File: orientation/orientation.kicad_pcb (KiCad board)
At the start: 2 copper layers, 45 x 30 mm, 9 parts, among them J1 Conn_01x02, J2 Conn_01x04, U1 Teensy4.0, U2 STSPIN220, U3 bno055

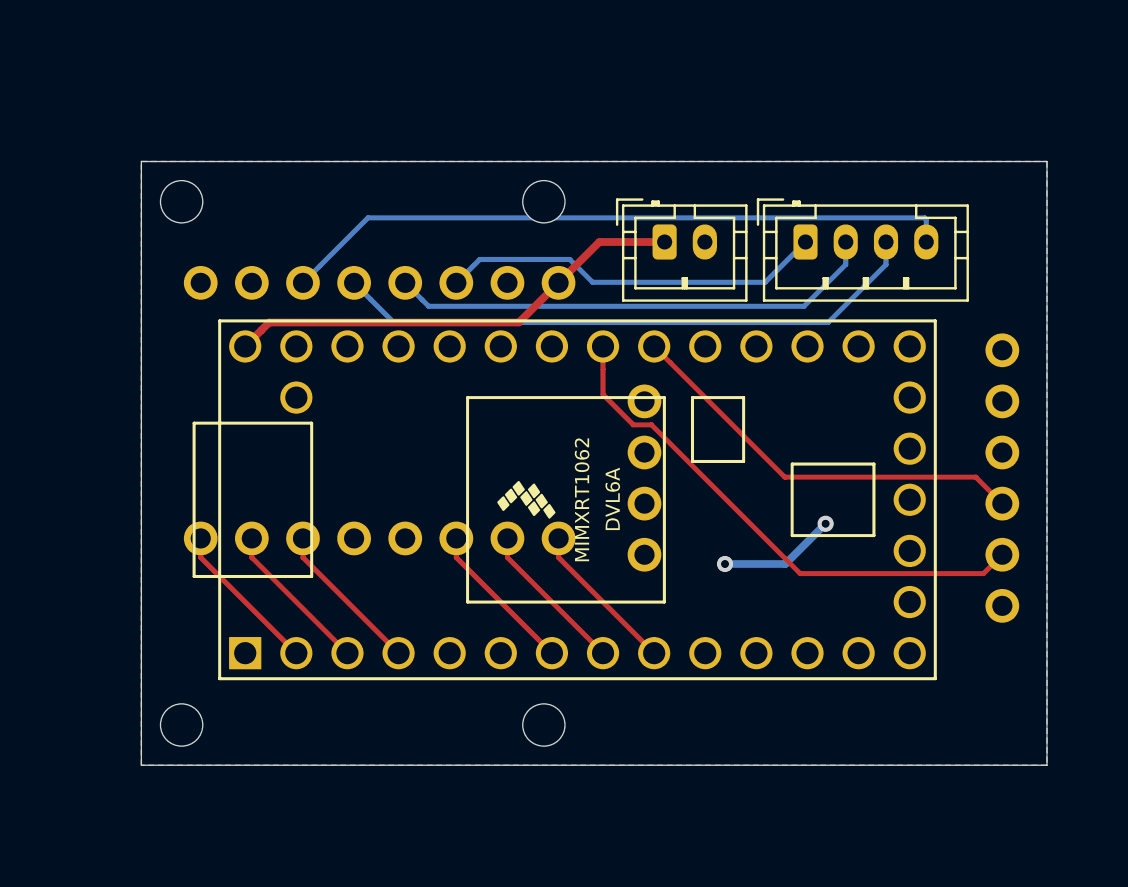
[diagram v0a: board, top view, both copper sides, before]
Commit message: add switch to orientation board
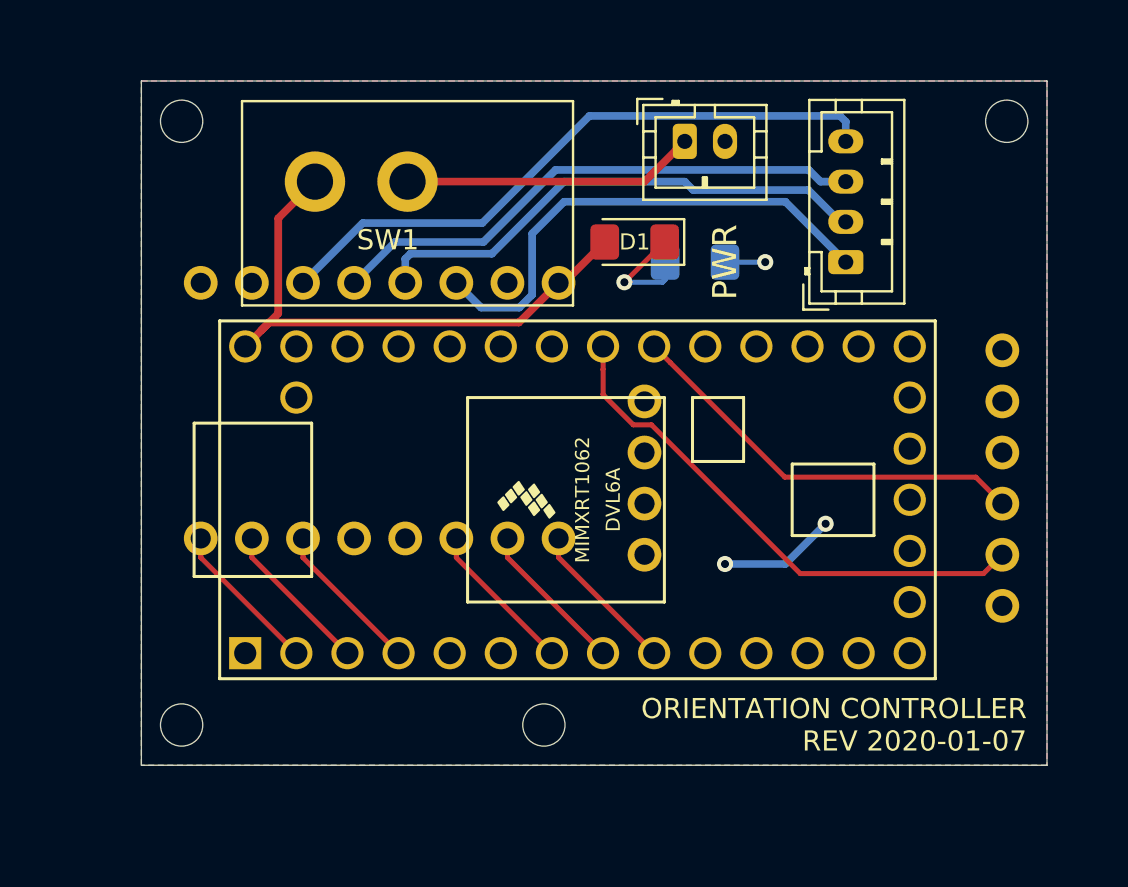
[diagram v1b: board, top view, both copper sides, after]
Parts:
- added D1: LED, LED_SMD:LED_1206_3216Metric_Pad1.42x1.75mm_HandSolder, F.Cu at (124.5, 66.0)
- added R1: 110, Resistor_SMD:R_1206_3216Metric_Pad1.42x1.75mm_HandSolder, B.Cu at (127.5, 67.0)
- added SW1: SW_SPST, NUSTARS:GF-123-0054, F.Cu at (105.0, 59.0)
- moved REF** 23.3 mm to (143.0, 60.0)
- moved J1 5.10 mm to (127.0, 61.0)
- moved REF** 4.00 mm to (102.0, 60.0)
- moved J2 2.24 mm to (135.0, 67.0), turned to 90 degrees
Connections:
- J1 pad 1: VBAT -> Net-(J1-Pad1)
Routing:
- net Net-(J1-Pad1): track 0.00 -> 14.6 mm
- net Net-(J2-Pad1): track 19.1 -> 25.1 mm
- net Net-(D1-Pad1): track 0.00 -> 5.78 mm, vias 0 -> 1
- net VBAT: track 23.0 -> 28.5 mm
- net Net-(J2-Pad3): track 29.6 -> 27.0 mm
- net GND: track 6.05 -> 8.05 mm, vias 2 -> 3
- net Net-(J2-Pad4): track 33.5 -> 31.5 mm
- net Net-(J2-Pad2): track 24.4 -> 25.5 mm
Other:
- board size 45 x 30 mm -> 45 x 34 mm
- board text added: "ORIENTATION CONTROLLER REV 2020-01-07"
- board text added: "PWR"

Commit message: updates
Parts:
- removed the REF** at (120.0, 90.0)
- removed the REF** at (143.0, 60.0)
- removed the REF** at (102.0, 60.0)
- removed the REF** at (102.0, 90.0)
- added REF**: MountingHole_3.2mm_M3, MountingHole:MountingHole_3.2mm_M3, F.Cu at (99.0, 92.0)
- added REF**: MountingHole_3.2mm_M3, MountingHole:MountingHole_3.2mm_M3, F.Cu at (143.0, 60.0)
- added REF**: MountingHole_3.2mm_M3, MountingHole:MountingHole_3.2mm_M3, F.Cu at (99.0, 60.0)
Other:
- board size 45 x 34 mm -> 52 x 40 mm
- board text added: "NUSTARS NSL ORIENTATION CONTROLLER REV 2020-01-12"
- board text removed: "ORIENTATION CONTROLLER REV 2020-01-07"
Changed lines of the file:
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@@
     (tracks 76)
     (zones 0)
-    (modules 12)
+    (modules 11)
     (nets 50)
   )
@@
     (add_net VBAT)
   )
+  (module MountingHole:MountingHole_3.2mm_M3 (layer F.Cu)
+    (at 99 92)
+    (descr "Mounting Hole 3.2mm, no annular, M3")
+    (tags "mounting hole 3.2mm no annular m3")
+    (attr virtual)
+    (fp_text reference REF** (at 0 -4.2) (layer F.SilkS) hide
+      (effects (font (size 1 1) (thickness 0.15)))
+    )
+    (fp_text value MountingHole_3.2mm_M3 (at 0 4.2) (layer F.Fab) hide
+      (effects (font (size 1 1) (thickness 0.15)))
+    )
+    (fp_circle (center 0 0) (end 3.45 0) (layer F.CrtYd) (width 0.05))
+    (fp_circle (center 0 0) (end 3.2 0) (layer Cmts.User) (width 0.15))
+    (fp_text user %R (at 0.3 0) (layer F.Fab)
+      (effects (font (size 1 1) (thickness 0.15)))
+    )
+    (pad 1 np_thru_hole circle (at 0 0) (size 3.2 3.2) (drill 3.2) (layers *.Cu *.Mask))
+  )
+  (module MountingHole:MountingHole_3.2mm_M3 (layer F.Cu)
+    (at 143 60)
+    (descr "Mounting Hole 3.2mm, no annular, M3")
+    (tags "mounting hole 3.2mm no annular m3")
+    (attr virtual)
+    (fp_text reference REF** (at 0 -4.2) (layer F.SilkS) hide
+      (effects (font (size 1 1) (thickness 0.15)))
+    )
+    (fp_text value MountingHole_3.2mm_M3 (at 0 4.2) (layer F.Fab) hide
+      (effects (font (size 1 1) (thickness 0.15)))
+    )
+    (fp_circle (center 0 0) (end 3.45 0) (layer F.CrtYd) (width 0.05))
+    (fp_circle (center 0 0) (end 3.2 0) (layer Cmts.User) (width 0.15))
+    (fp_text user %R (at 0.3 0) (layer F.Fab)
+      (effects (font (size 1 1) (thickness 0.15)))
+    )
+    (pad 1 np_thru_hole circle (at 0 0) (size 3.2 3.2) (drill 3.2) (layers *.Cu *.Mask))
+  )
+  (module MountingHole:MountingHole_3.2mm_M3 (layer F.Cu)
+    (at 99 60)
+    (descr "Mounting Hole 3.2mm, no annular, M3")
+    (tags "mounting hole 3.2mm no annular m3")
+    (attr virtual)
+    (fp_text reference REF** (at 0 -4.2) (layer F.SilkS) hide
+      (effects (font (size 1 1) (thickness 0.15)))
+    )
+    (fp_text value MountingHole_3.2mm_M3 (at 0 4.2) (layer F.Fab) hide
+      (effects (font (size 1 1) (thickness 0.15)))
+    )
+    (fp_circle (center 0 0) (end 3.45 0) (layer F.CrtYd) (width 0.05))
+    (fp_circle (center 0 0) (end 3.2 0) (layer Cmts.User) (width 0.15))
+    (fp_text user %R (at 0.3 0) (layer F.Fab)
+      (effects (font (size 1 1) (thickness 0.15)))
+    )
+    (pad 1 np_thru_hole circle (at 0 0) (size 3.2 3.2) (drill 3.2) (layers *.Cu *.Mask))
+  )
   (module NUSTARS:GF-123-0054 (layer F.Cu)
     (at 105 59)
@@
     (pad 6 thru_hole circle (at 19.685 -19.05 270) (size 1.6764 1.6764) (drill 1) (layers *.Cu *.Mask)
       (net 41 "Net-(U3-Pad6)"))
-  )
-  (module MountingHole:MountingHole_2.1mm (layer F.Cu)
-    (at 120 90)
-    (descr "Mounting Hole 2.1mm, no annular")
-    (tags "mounting hole 2.1mm no annular")
-    (attr virtual)
-    (fp_text reference REF** (at 0 -3.2) (layer F.SilkS) hide
-      (effects (font (size 1 1) (thickness 0.15)))
-    )
-    (fp_text value MountingHole_2.1mm (at 0 3.2) (layer F.Fab) hide
-      (effects (font (size 1 1) (thickness 0.15)))
-    )
-    (fp_circle (center 0 0) (end 2.35 0) (layer F.CrtYd) (width 0.05))
-    (fp_circle (center 0 0) (end 2.1 0) (layer Cmts.User) (width 0.15))
-    (pad "" np_thru_hole circle (at 0 0) (size 2.1 2.1) (drill 2.1) (layers *.Cu *.Mask))
-  )
-  (module MountingHole:MountingHole_2.1mm (layer F.Cu)
-    (at 143 60)
-    (descr "Mounting Hole 2.1mm, no annular")
-    (tags "mounting hole 2.1mm no annular")
-    (attr virtual)
-    (fp_text reference REF** (at -9 0) (layer F.SilkS) hide
-      (effects (font (size 1 1) (thickness 0.15)))
-    )
-    (fp_text value MountingHole_2.1mm (at 0 3.2) (layer F.Fab) hide
-      (effects (font (size 1 1) (thickness 0.15)))
-    )
-    (fp_circle (center 0 0) (end 2.35 0) (layer F.CrtYd) (width 0.05))
-    (fp_circle (center 0 0) (end 2.1 0) (layer Cmts.User) (width 0.15))
-    (pad "" np_thru_hole circle (at 0 0) (size 2.1 2.1) (drill 2.1) (layers *.Cu *.Mask))
-  )
-  (module MountingHole:MountingHole_2.1mm (layer F.Cu)
-    (at 102 60)
-    (descr "Mounting Hole 2.1mm, no annular")
-    (tags "mounting hole 2.1mm no annular")
-    (attr virtual)
-    (fp_text reference REF** (at 0 -3.2) (layer F.SilkS) hide
-      (effects (font (size 1 1) (thickness 0.15)))
-    )
-    (fp_text value MountingHole_2.1mm (at 0 3.2) (layer F.Fab) hide
-      (effects (font (size 1 1) (thickness 0.15)))
-    )
-    (fp_circle (center 0 0) (end 2.35 0) (layer F.CrtYd) (width 0.05))
-    (fp_circle (center 0 0) (end 2.1 0) (layer Cmts.User) (width 0.15))
-    (pad "" np_thru_hole circle (at 0 0) (size 2.1 2.1) (drill 2.1) (layers *.Cu *.Mask))
-  )
-  (module MountingHole:MountingHole_2.1mm (layer F.Cu)
-    (at 102 90)
-    (descr "Mounting Hole 2.1mm, no annular")
-    (tags "mounting hole 2.1mm no annular")
-    (attr virtual)
-    (fp_text reference REF** (at 0 -3.2) (layer F.SilkS) hide
-      (effects (font (size 1 1) (thickness 0.15)))
-    )
-    (fp_text value MountingHole_2.1mm (at 0 3.2) (layer F.Fab) hide
-      (effects (font (size 1 1) (thickness 0.15)))
-    )
-    (fp_circle (center 0 0) (end 2.35 0) (layer F.CrtYd) (width 0.05))
-    (fp_circle (center 0 0) (end 2.1 0) (layer Cmts.User) (width 0.15))
-    (pad "" np_thru_hole circle (at 0 0) (size 2.1 2.1) (drill 2.1) (layers *.Cu *.Mask))
   )
   (module Connector_JST:JST_PH_B4B-PH-K_1x04_P2.00mm_Vertical (layer F.Cu)
@@
     (effects (font (size 1.2 1.2) (thickness 0.15)))
   )
-  (gr_text "ORIENTATION CONTROLLER\nREV 2020-01-07" (at 144 90) (layer F.SilkS)
+  (gr_text "NUSTARS NSL\nORIENTATION CONTROLLER\nREV 2020-01-12" (at 144 92) (layer F.SilkS)
     (effects (font (size 1 1) (thickness 0.15)) (justify right))
   )
-  (dimension 45 (width 0.15) (layer F.Fab)
-    (gr_text "45.000 mm" (at 122.5 95.3) (layer F.Fab)
-      (effects (font (size 1 1) (thickness 0.15)))
-    )
-    (feature1 (pts (xy 145 92) (xy 145 94.586421)))
-    (feature2 (pts (xy 100 92) (xy 100 94.586421)))
-    (crossbar (pts (xy 100 94) (xy 145 94)))
-    (arrow1a (pts (xy 145 94) (xy 143.873496 94.586421)))
-    (arrow1b (pts (xy 145 94) (xy 143.873496 93.413579)))
-    (arrow2a (pts (xy 100 94) (xy 101.126504 94.586421)))
-    (arrow2b (pts (xy 100 94) (xy 101.126504 93.413579)))
-  )
-  (dimension 34 (width 0.15) (layer F.Fab)
-    (gr_text "34.000 mm" (at 149.3 75 270) (layer F.Fab)
-      (effects (font (size 1 1) (thickness 0.15)))
-    )
-    (feature1 (pts (xy 145 92) (xy 148.586421 92)))
-    (feature2 (pts (xy 145 58) (xy 148.586421 58)))
-    (crossbar (pts (xy 148 58) (xy 148 92)))
-    (arrow1a (pts (xy 148 92) (xy 147.413579 90.873496)))
-    (arrow1b (pts (xy 148 92) (xy 148.586421 90.873496)))
-    (arrow2a (pts (xy 148 58) (xy 147.413579 59.126504)))
-    (arrow2b (pts (xy 148 58) (xy 148.586421 59.126504)))
-  )
-  (gr_line (start 145 92) (end 145 58) (layer Edge.Cuts) (width 0.05))
-  (gr_line (start 100 92) (end 145 92) (layer Edge.Cuts) (width 0.05))
-  (gr_line (start 100 58) (end 100 92) (layer Edge.Cuts) (width 0.05))
-  (gr_line (start 145 58) (end 100 58) (layer Edge.Cuts) (width 0.05))
+  (dimension 52 (width 0.15) (layer F.Fab)
+    (gr_text "52.000 mm" (at 121 99.3) (layer F.Fab)
+      (effects (font (size 1 1) (thickness 0.15)))
+    )
+    (feature1 (pts (xy 147 96) (xy 147 98.586421)))
+    (feature2 (pts (xy 95 96) (xy 95 98.586421)))
+    (crossbar (pts (xy 95 98) (xy 147 98)))
+    (arrow1a (pts (xy 147 98) (xy 145.873496 98.586421)))
+    (arrow1b (pts (xy 147 98) (xy 145.873496 97.413579)))
+    (arrow2a (pts (xy 95 98) (xy 96.126504 98.586421)))
+    (arrow2b (pts (xy 95 98) (xy 96.126504 97.413579)))
+  )
+  (dimension 40 (width 0.15) (layer F.Fab)
+    (gr_text "40.000 mm" (at 151.3 76 270) (layer F.Fab)
+      (effects (font (size 1 1) (thickness 0.15)))
+    )
+    (feature1 (pts (xy 147 96) (xy 150.586421 96)))
+    (feature2 (pts (xy 147 56) (xy 150.586421 56)))
+    (crossbar (pts (xy 150 56) (xy 150 96)))
+    (arrow1a (pts (xy 150 96) (xy 149.413579 94.873496)))
+    (arrow1b (pts (xy 150 96) (xy 150.586421 94.873496)))
+    (arrow2a (pts (xy 150 56) (xy 149.413579 57.126504)))
+    (arrow2b (pts (xy 150 56) (xy 150.586421 57.126504)))
+  )
+  (gr_line (start 147 96) (end 147 56) (layer Edge.Cuts) (width 0.05))
+  (gr_line (start 95 96) (end 147 96) (layer Edge.Cuts) (width 0.05))
+  (gr_line (start 95 56) (end 95 96) (layer Edge.Cuts) (width 0.05))
+  (gr_line (start 147 56) (end 95 56) (layer Edge.Cuts) (width 0.05))
   (segment (start 105 86.59) (end 105.16 86.43) (width 0.25) (layer F.Cu) (net 1))
   (via (at 134 80) (size 0.8) (drill 0.4) (layers F.Cu B.Cu) (net 1))
@@
     (polygon
       (pts
-        (xy 145 92) (xy 100 92) (xy 100 58) (xy 145 58)
+        (xy 146 95) (xy 96 95) (xy 96 57) (xy 146 57)
       )
     )
@@
     (polygon
       (pts
-        (xy 145 92) (xy 100 92) (xy 100 58) (xy 145 58)
+        (xy 146 95) (xy 96 95) (xy 96 57) (xy 146 57)
       )
     )

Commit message: prelim finish sans decor
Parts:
- added G***: LOGO, NUSTARS:decorative_rotate, F.Cu at (107.9, 91.6)
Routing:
- net GND: track 8.05 -> 4.73 mm
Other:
- board text added: "NUSTARS NSL ORIENTATION CONTROLLER REV 2020-01-18"
- board text removed: "NUSTARS NSL ORIENTATION CONTROLLER REV 2020-01-12"

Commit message: add GND and 3.3V connections on orientation
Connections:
- U2 pad 10: Net-(U2-Pad10) -> 3V3T
- U2 pad 9: Net-(U2-Pad9) -> GND
- U3 pad 3: Net-(U3-Pad3) -> GND
